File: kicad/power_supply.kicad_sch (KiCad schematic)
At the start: 24 parts, among them T1 reuse / AnTek AS-0524, U1 LM317T

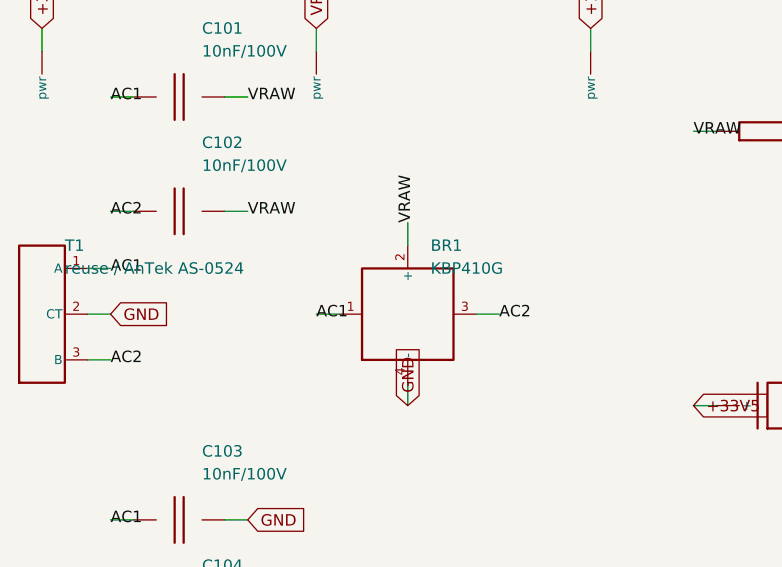
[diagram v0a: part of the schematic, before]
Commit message: Datasheet footprints, floor-plan placement, headless autoroute (144/145, DRC 0)
PCB-AUDIT s1 fixes with datasheet-derived project footprints:
- TO-220-5_Vertical_P1.70mm_LM1875 (TI NDH0005D): 1.45 mm pads on the 1.1 mm
  drill -> 0.175 mm annular (was 0.0875, 5 DRC errors); pad-local 0.2 mm clearance
- Bridge_KBP_P3.81mm (Diodes DS39310 KBP404G-KBP410G, pins + ~ ~ -); bridge
  symbol renumbered to the physical order; errata #3 updated (KBU needs a swap)
- value-aware CP/R sizing (real can sizes for 4700/2200/1000 uF, 5 W / 1 W
  resistors, fat pads on the 0R speaker return); Part 4 wire pads for all
  off-board wiring (2.0 mm/1.2 mm signal, 3.0 mm/1.5 mm speaker + transformer)
- VRAW/AC1/AC2 moved into the HighCurrent net class (errata #11)

gen_pcb.py now places to the Part 5 floor plan: balanced columns (Input/Preamp
with Tone stacked below | Reverb/Trem/MRB | Power Amp | PSU), signal order inside
zones with serpentine shelves, LM1875/LM317 on the top edge with the 10 mm
keep-out, wiring edge along the bottom, 4x M3 holes, two locked 0.9 mm escape
stubs off the LM1875 pins 4/5 (a 1.5/2.5 mm trace cannot enter a 1.70 mm pitch).
DRC before routing: 0 errors, 0 warnings.

route_board.py: pcbnew DSN export -> Freerouting -> SES import -> pour refill.
Freerouting 2.1.0 ignores every pass/timeout limit in CLI mode and only writes
output at 0 unrouted (and its MT router crashed), so the script drives 1.9.0
under xvfb-run and injects autoroute_settings (bottom layer 6x cost, via 80) so
the GND pour stays whole. Committed board: 144/145 connections routed, 0 DRC
violations (--severity-all), 26 vias, 351 mm on the bottom vs 3.7 m on top; the
one open PA_OUT link (blocked by R_bias1) is documented as a GUI finish.

Chassis-fit figure corrected: the old 48-53 % / 82-90 % densities counted hidden
text boxes; text-less it is ~33 % on 190x115 and ~56 % on 155x90.

Docs: PCB-NOTES/PCB-AUDIT rewritten, README, CHANGELOG, errata #3/#11,
SOURCES (package drawings), Part 10, kicad RE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
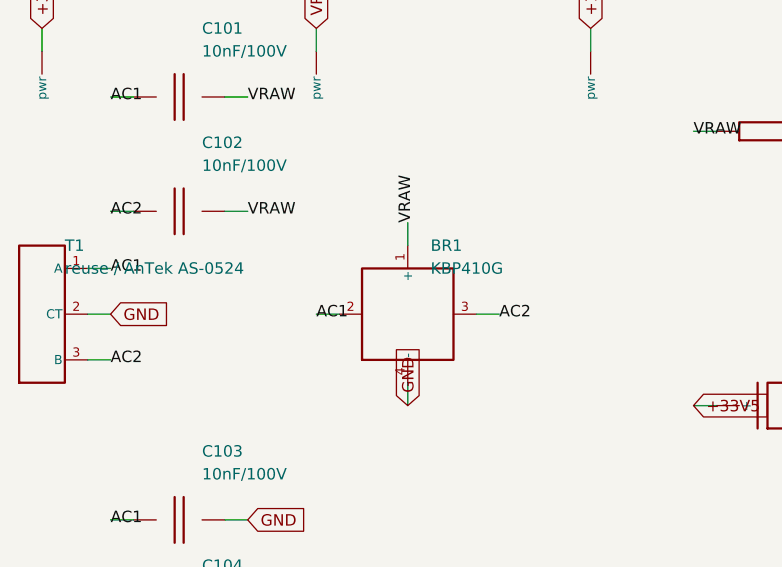
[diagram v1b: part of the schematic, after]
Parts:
- BR1: footprint Connector_PinHeader_2.54mm:PinHeader_1x04_P2.54mm_Vertical -> cambridge_reverb:Bridge_KBP_P3.81mm
- C_filt1, C_filt2: footprint Capacitor_THT:CP_Radial_D8.0mm_P3.50mm -> Capacitor_THT:CP_Radial_D12.5mm_P5.00mm
- C_main: footprint Capacitor_THT:CP_Radial_D8.0mm_P3.50mm -> Capacitor_THT:CP_Radial_D18.0mm_P7.50mm
- C_reg_in, C_reg_out1: footprint Capacitor_THT:CP_Radial_D8.0mm_P3.50mm -> Capacitor_THT:CP_Radial_D5.0mm_P2.50mm
- C_vbr, C_vbt: footprint Capacitor_THT:CP_Radial_D8.0mm_P3.50mm -> Capacitor_THT:CP_Radial_D6.3mm_P2.50mm
- R_27V: footprint Resistor_THT:R_Axial_DIN0207_L6.3mm_D2.5mm_P5.08mm_Vertical -> Resistor_THT:R_Axial_DIN0414_L11.9mm_D4.5mm_P15.24mm_Horizontal
- R_bleed: footprint Resistor_THT:R_Axial_DIN0207_L6.3mm_D2.5mm_P5.08mm_Vertical -> Resistor_THT:R_Axial_Power_L20.0mm_W6.4mm_P25.40mm
- T1: footprint Connector_PinHeader_2.54mm:PinHeader_1x03_P2.54mm_Vertical -> cambridge_reverb:WirePad_1x03_P5.08mm_D1.5mm
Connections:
- net AC1: now also BR1.2; no longer BR1.1
- net VRAW: now also BR1.1 (+); no longer BR1.2 (+)

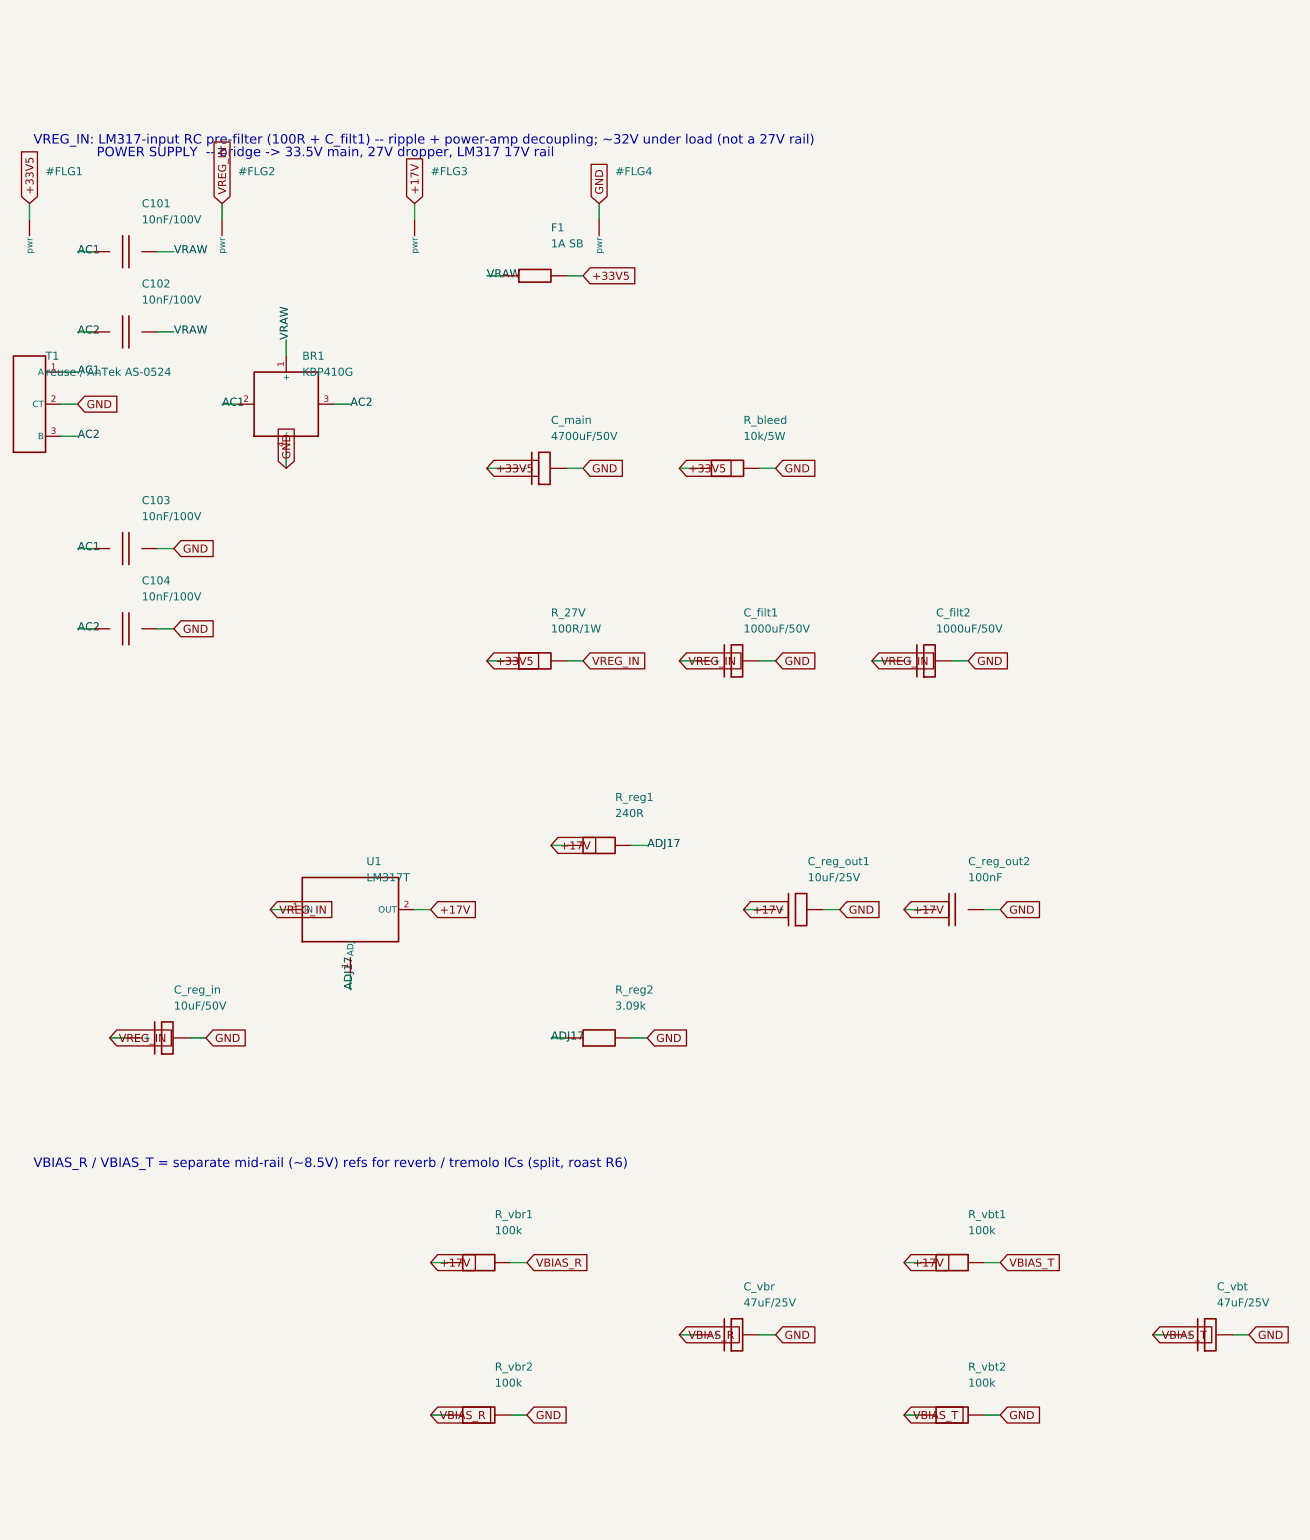
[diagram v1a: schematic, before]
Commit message: Add 26 labelled bench test points (schematic + BOM + silk) and re-route
Test points follow the Part 5 bring-up order: rails (VRAW, +33V5, VREG_IN,
+17V), JFET drains Q1D/Q2D/QRD (the errata #15 bias trim), the VBIAS_R/VBIAS_T
mid-rail refs, every inter-stage node (PREAMP_OUT, TONE_OUT, BLEND, TREM_OUT,
MRB_OUT, PA_IN), tank drive/return, LFO, PA_BIAS/PA_OUT/SPK_P, and a GND pin
per zone for the probe clip.

- gen_kicad.py: one-pin TP symbol; TEST_POINTS table; add_test_points() puts
  them on their sheets so they are in the netlist and the BOM (one order line)
- footprint TestPoint_THT_D2.0mm_Label: 2.0 mm pad / 1.0 mm drill for a header
  pin or wire loop; the footprint VALUE (= net alias) prints on F.SilkS
- gen_pcb.py: test-point strip across the top of each zone; the effects column
  is now two stacked zones (tremolo+MRB above, reverb below next to its tank
  pads) so each block's points sit right above its parts; stacked-zone gap 2 mm
- PCB-NOTES.md: test-point table with expected values (Part 3 troubleshooting,
  Part 2 set-up, ngspice) and the bring-up sequence
- Re-routed (Freerouting 1.9.0, B.Cu x7, via 60): 161/166 connections, 0 DRC
  violations, 54 vias; the five open links are listed for a GUI finish

Co-Authored-By: Claude Fable 5.1 <noreply@anthropic.com>
Claude-Session: https://claude.ai/code/session_01Vk8HkvCugxFpQsBPVnNT2H
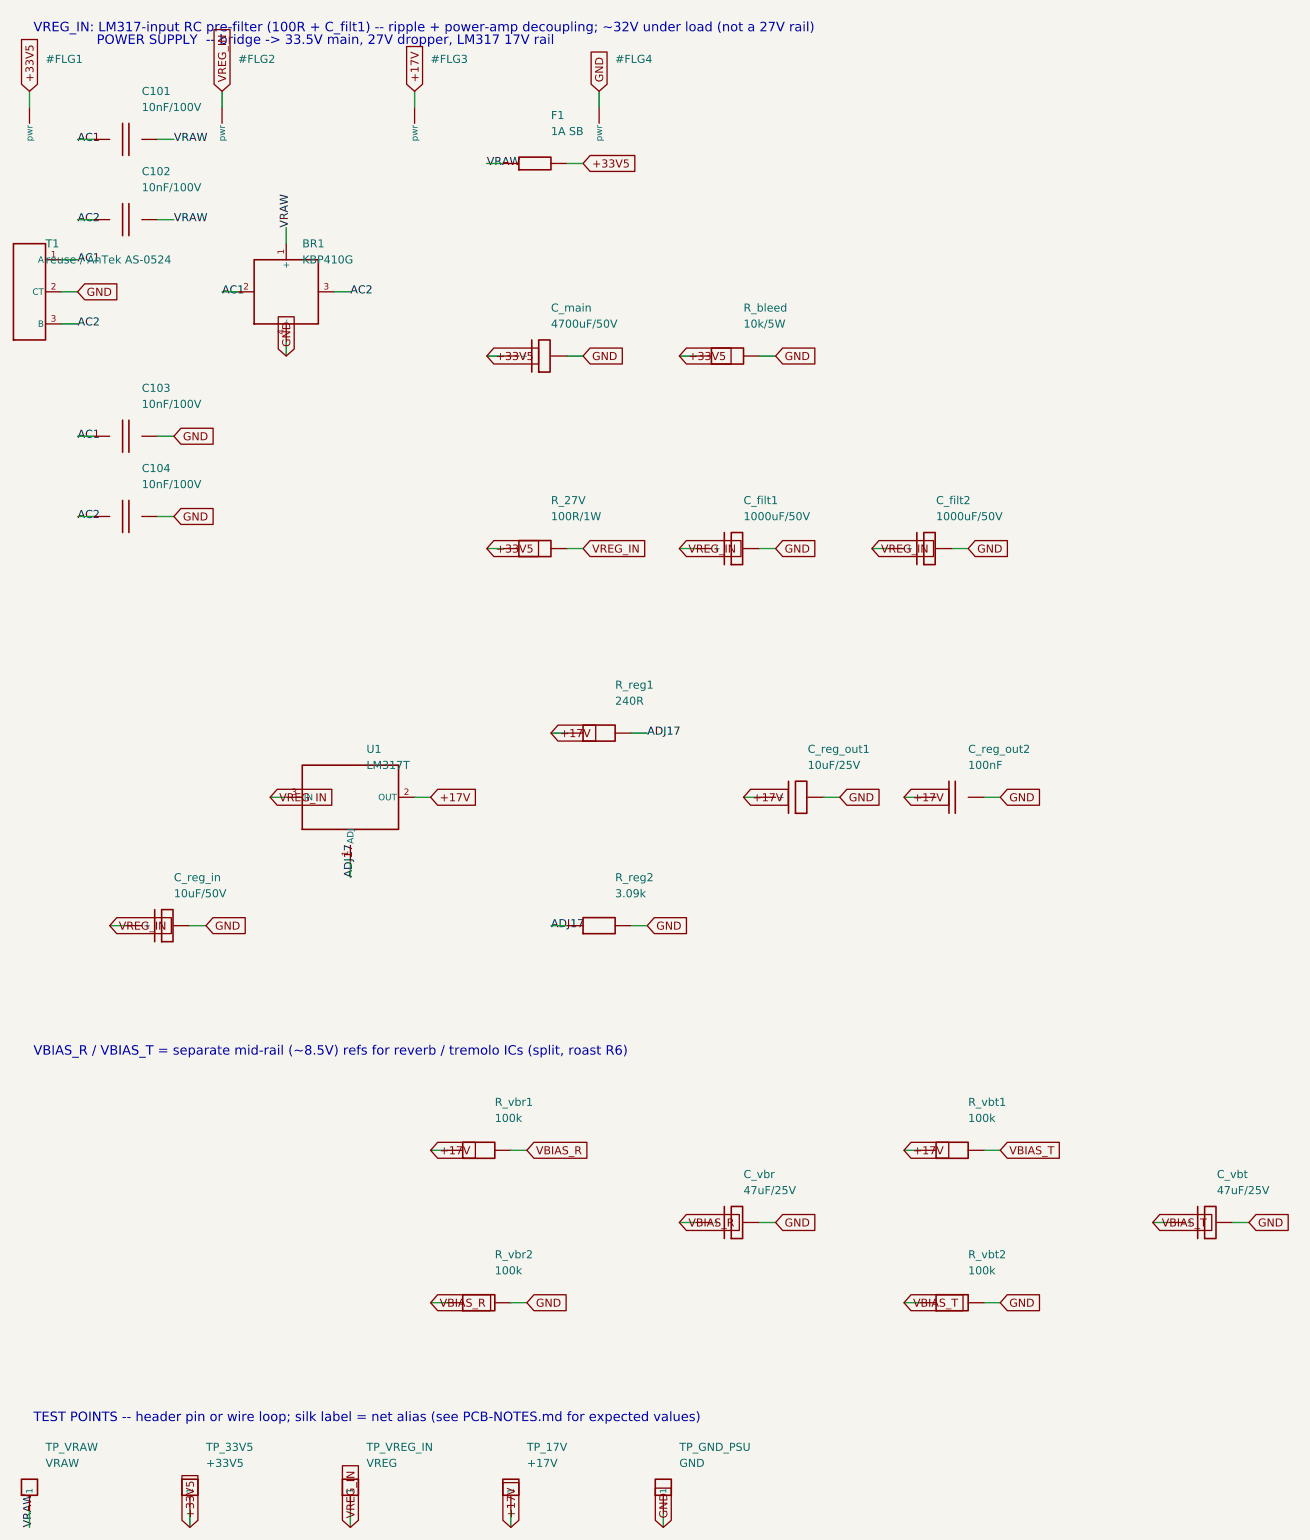
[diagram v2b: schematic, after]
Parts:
- added TP_17V: +17V, cambridge_reverb:TestPoint_THT_D2.0mm_Label, symbol cr_primitives:TP
- added TP_33V5: +33V5, cambridge_reverb:TestPoint_THT_D2.0mm_Label, symbol cr_primitives:TP
- added TP_GND_PSU: GND, cambridge_reverb:TestPoint_THT_D2.0mm_Label, symbol cr_primitives:TP
- added TP_VRAW: VRAW, cambridge_reverb:TestPoint_THT_D2.0mm_Label, symbol cr_primitives:TP
- added TP_VREG_IN: VREG, cambridge_reverb:TestPoint_THT_D2.0mm_Label, symbol cr_primitives:TP
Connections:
- net +17V: now also TP_17V.1
- net +33V5: now also TP_33V5.1
- net GND: now also TP_GND_PSU.1
- net VRAW: now also TP_VRAW.1
- net VREG_IN: now also TP_VREG_IN.1
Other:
- note added: "TEST POINTS -- header pin or wire loop; silk label = net alias (see PCB-NOTES.md for expected values)"
